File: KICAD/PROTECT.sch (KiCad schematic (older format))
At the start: 0 parts

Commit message: labels dans les blocks
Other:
- note added: "Bidir"
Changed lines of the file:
@@
 $Descr A4 11693 8268
 encoding utf-8
-Sheet 1 15
+Sheet 6 15
 Title ""
 Date ""
@@
 Comment4 ""
 $EndDescr
+Text HLabel 2700 3050 0    100  BiDi ~ 0
+IN_OUT_PWR
+Text HLabel 2700 3250 0    100  BiDi ~ 0
+VProt
+Text Notes 2300 3500 0    100  ~ 0
+Bidir
+Wire Notes Line
+	2800 2950 2800 3600
+Wire Notes Line
+	2800 3600 1600 3600
+Wire Notes Line
+	1600 3600 1600 2950
+Wire Notes Line
+	1600 2950 2800 2950
 $EndSCHEMATC

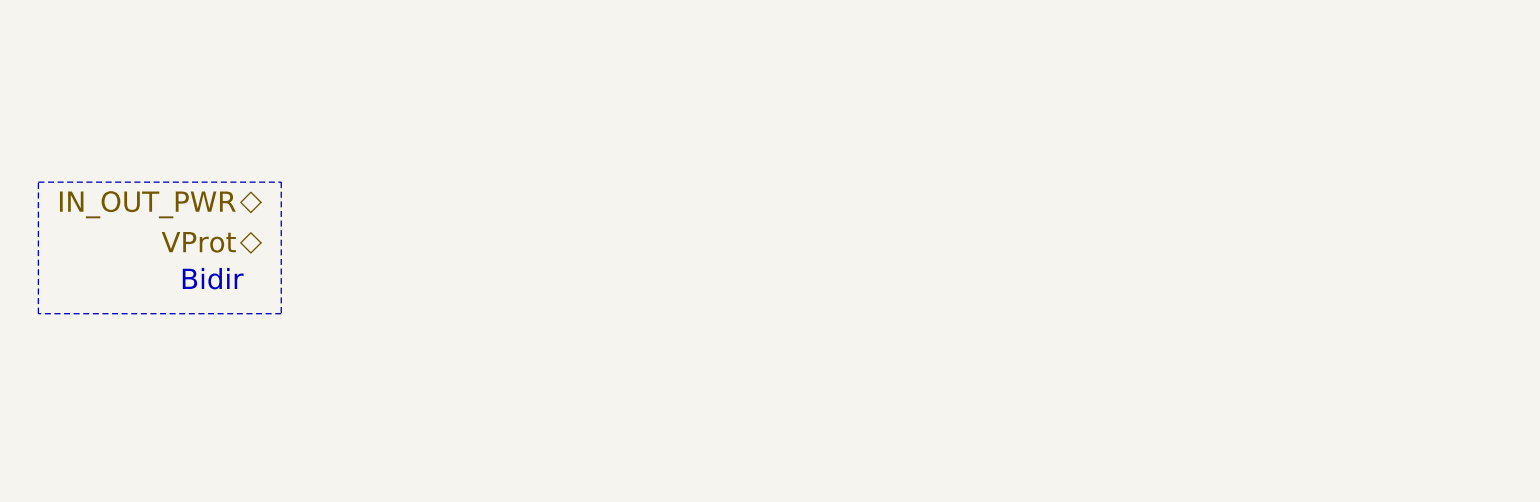
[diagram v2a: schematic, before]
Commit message: added ina240 sim + drawed protect and DC-DC chopper
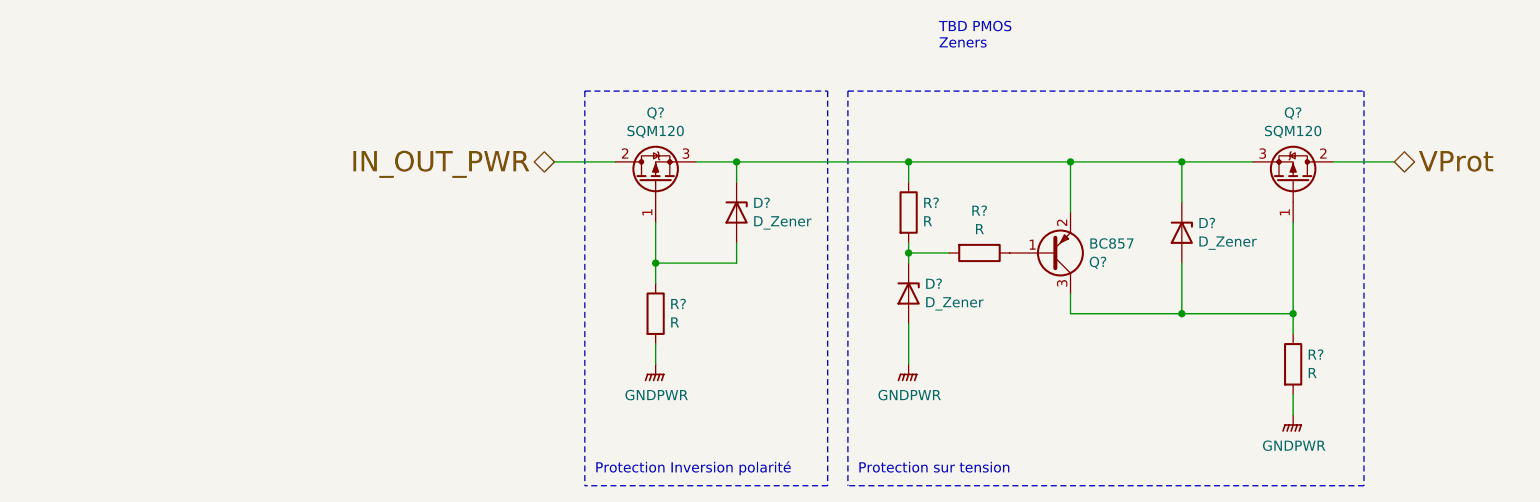
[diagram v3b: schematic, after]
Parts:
- added D? (x3): D_Zener, symbol Device:D_Zener
- added Q? (x2): SQM120, symbol Device:Q_PMOS_GDS
- added Q?: BC857, Package_TO_SOT_SMD:SOT-23, symbol Transistor_BJT:BC857
- added R? (x4): R, symbol Device:R
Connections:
- net IN_OUT_PWR: now also Q?.2 (D)
- net VProt: now also Q?.2 (D)
- new net: D?.2 (A), Q?.1 (G), R?.1
- new net: D?.1 (K), D?.1 (K), Q?.2 (E), Q?.3 (S), Q?.3 (S), R?.1
- new net: D?.2 (A), Q?.1 (G), Q?.3 (C), R?.1
- new net: Q?.1 (B), R?.1
- new net: D?.1 (K), R?.2, R?.2
- new net GNDPWR: D?.2 (A), R?.2, R?.2
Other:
- note added: "Protection Inversion polarité"
- note added: "Protection sur tension"
- note added: "TBD PMOS\nZeners\n"
- note removed: "Bidir"
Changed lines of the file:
@@
 $Descr A4 11693 8268
 encoding utf-8
-Sheet 6 15
+Sheet 5 15
 Title ""
 Date ""
 Rev ""
 Comp "ALEEA"
-Comment1 ""
+Comment1 "Dessin : Guillaume Arthaud"
 Comment2 ""
 Comment3 ""
 Comment4 ""
 $EndDescr
-Text HLabel 2700 3050 0    100  BiDi ~ 0
+Text HLabel 4150 2850 0    100  BiDi ~ 0
 IN_OUT_PWR
-Text HLabel 2700 3250 0    100  BiDi ~ 0
+Text HLabel 8300 2850 2    100  BiDi ~ 0
 VProt
-Text Notes 2300 3500 0    100  ~ 0
-Bidir
-Wire Notes Line
-	2800 2950 2800 3600
-Wire Notes Line
-	2800 3600 1600 3600
-Wire Notes Line
-	1600 3600 1600 2950
-Wire Notes Line
-	1600 2950 2800 2950
+$Comp
+L Device:Q_PMOS_GDS Q?
+U 1 1 610FCCAA
+P 4650 2950
+F 0 "Q?" V 4992 2950 50  0000 C CNN
+F 1 "SQM120" V 4901 2950 50  0000 C CNN
+F 2 "" H 4850 3050 50  0001 C CNN
+F 3 "~" H 4650 2950 50  0001 C CNN
+	1    4650 2950
+	0    -1   -1   0
+$EndComp
+$Comp
+L Device:Q_PMOS_GDS Q?
+U 1 1 610FED91
+P 7800 2950
+F 0 "Q?" V 8142 2950 50  0000 C CNN
+F 1 "SQM120" V 8051 2950 50  0000 C CNN
+F 2 "" H 8000 3050 50  0001 C CNN
+F 3 "~" H 7800 2950 50  0001 C CNN
+	1    7800 2950
+	0    1    -1   0
+$EndComp
+$Comp
+L Device:D_Zener D?
+U 1 1 61100A0F
+P 5050 3100
+F 0 "D?" V 5004 3180 50  0000 L CNN
+F 1 "D_Zener" V 5095 3180 50  0000 L CNN
+F 2 "" H 5050 3100 50  0001 C CNN
+F 3 "~" H 5050 3100 50  0001 C CNN
+	1    5050 3100
+	0    1    1    0
+$EndComp
+Wire Wire Line
+	4850 2850 5050 2850
+$Comp
+L Device:R R?
+U 1 1 61102FC8
+P 4650 3600
+F 0 "R?" H 4720 3646 50  0000 L CNN
+F 1 "R" H 4720 3555 50  0000 L CNN
+F 2 "" V 4580 3600 50  0001 C CNN
+F 3 "~" H 4650 3600 50  0001 C CNN
+	1    4650 3600
+	1    0    0    -1
+$EndComp
+Wire Wire Line
+	5050 2950 5050 2850
+Wire Wire Line
+	5050 3250 5050 3350
+Wire Wire Line
+	5050 3350 4650 3350
+Wire Wire Line
+	4650 3350 4650 3150
+Wire Wire Line
+	4650 3450 4650 3350
+Connection ~ 4650 3350
+$Comp
+L power:GNDPWR #PWR?
+U 1 1 61104B6E
+P 4650 3850
+F 0 "#PWR?" H 4650 3650 50  0001 C CNN
+F 1 "GNDPWR" H 4654 3696 50  0000 C CNN
+F 2 "" H 4650 3800 50  0001 C CNN
+F 3 "" H 4650 3800 50  0001 C CNN
+	1    4650 3850
+	1    0    0    -1
+$EndComp
+Wire Wire Line
+	4650 3850 4650 3750
+Wire Wire Line
+	4150 2850 4450 2850
+Wire Notes Line
+	4300 2500 5500 2500
+Connection ~ 5050 2850
+$Comp
+L Transistor_BJT:BC857 Q?
+U 1 1 6110710F
+P 6600 3300
+F 0 "Q?" H 6791 3346 50  0000 L CNN
+F 1 "BC857" H 6791 3255 50  0000 L CNN
+F 2 "Package_TO_SOT_SMD:SOT-23" H 6800 3225 50  0001 L CIN
+F 3 "https://www.onsemi.com/pub/Collateral/BC860-D.pdf" H 6600 3300 50  0001 L CNN
+	1    6600 3300
+	1    0    0    1
+$EndComp
+$Comp
+L Device:D_Zener D?
+U 1 1 61107C25
+P 5900 3500
+F 0 "D?" V 5854 3580 50  0000 L CNN
+F 1 "D_Zener" V 5945 3580 50  0000 L CNN
+F 2 "" H 5900 3500 50  0001 C CNN
+F 3 "~" H 5900 3500 50  0001 C CNN
+	1    5900 3500
+	0    1    1    0
+$EndComp
+$Comp
+L Device:D_Zener D?
+U 1 1 61107DEE
+P 7250 3200
+F 0 "D?" V 7204 3280 50  0000 L CNN
+F 1 "D_Zener" V 7295 3280 50  0000 L CNN
+F 2 "" H 7250 3200 50  0001 C CNN
+F 3 "~" H 7250 3200 50  0001 C CNN
+	1    7250 3200
+	0    1    1    0
+$EndComp
+$Comp
+L Device:R R?
+U 1 1 611083FB
+P 5900 3100
+F 0 "R?" H 5970 3146 50  0000 L CNN
+F 1 "R" H 5970 3055 50  0000 L CNN
+F 2 "" V 5830 3100 50  0001 C CNN
+F 3 "~" H 5900 3100 50  0001 C CNN
+	1    5900 3100
+	1    0    0    -1
+$EndComp
+Wire Wire Line
+	5900 3250 5900 3300
+Wire Wire Line
+	5900 2950 5900 2850
+Wire Wire Line
+	5050 2850 5900 2850
+$Comp
+L Device:R R?
+U 1 1 6110B925
+P 6250 3300
+F 0 "R?" V 6043 3300 50  0000 C CNN
+F 1 "R" V 6134 3300 50  0000 C CNN
+F 2 "" V 6180 3300 50  0001 C CNN
+F 3 "~" H 6250 3300 50  0001 C CNN
+	1    6250 3300
+	0    1    1    0
+$EndComp
+Wire Wire Line
+	6100 3300 5900 3300
+Connection ~ 5900 3300
+Wire Wire Line
+	5900 3300 5900 3350
+Wire Wire Line
+	5900 2850 6700 2850
+Wire Wire Line
+	6700 2850 6700 3100
+Connection ~ 5900 2850
+Wire Wire Line
+	7250 2850 6700 2850
+Connection ~ 6700 2850
+Wire Wire Line
+	6700 3600 6700 3500
+Wire Wire Line
+	7600 2850 7250 2850
+Connection ~ 7250 2850
+$Comp
+L Device:R R?
+U 1 1 61115761
+P 7800 3850
+F 0 "R?" H 7870 3896 50  0000 L CNN
+F 1 "R" H 7870 3805 50  0000 L CNN
+F 2 "" V 7730 3850 50  0001 C CNN
+F 3 "~" H 7800 3850 50  0001 C CNN
+	1    7800 3850
+	1    0    0    -1
+$EndComp
+$Comp
+L power:GNDPWR #PWR?
+U 1 1 6111576B
+P 7800 4100
+F 0 "#PWR?" H 7800 3900 50  0001 C CNN
+F 1 "GNDPWR" H 7804 3946 50  0000 C CNN
+F 2 "" H 7800 4050 50  0001 C CNN
+F 3 "" H 7800 4050 50  0001 C CNN
+	1    7800 4100
+	1    0    0    -1
+$EndComp
+Wire Wire Line
+	7800 4100 7800 4000
+$Comp
+L power:GNDPWR #PWR?
+U 1 1 611168C4
+P 5900 3850
+F 0 "#PWR?" H 5900 3650 50  0001 C CNN
+F 1 "GNDPWR" H 5904 3696 50  0000 C CNN
+F 2 "" H 5900 3800 50  0001 C CNN
+F 3 "" H 5900 3800 50  0001 C CNN
+	1    5900 3850
+	1    0    0    -1
+$EndComp
+Wire Wire Line
+	5900 3650 5900 3850
+Wire Wire Line
+	7800 3700 7800 3600
+Wire Wire Line
+	7800 3150 7800 3600
+Connection ~ 7800 3600
+Wire Wire Line
+	6700 3600 7250 3600
+Wire Wire Line
+	7250 3350 7250 3600
+Connection ~ 7250 3600
+Wire Wire Line
+	7250 3600 7800 3600
+Wire Wire Line
+	7250 2850 7250 3050
+Wire Notes Line
+	5600 2500 8150 2500
+Wire Notes Line
+	8150 4450 5600 4450
+Wire Notes Line
+	8150 2500 8150 4450
+Wire Notes Line
+	5600 2500 5600 4450
+Text Notes 5650 4400 0    50   ~ 0
+Protection sur tension
+Text Notes 4350 4400 0    50   ~ 0
+Protection Inversion polarité
+Wire Notes Line
+	5500 4450 4300 4450
+Wire Notes Line
+	5500 2500 5500 4450
+Wire Notes Line
+	4300 2500 4300 4450
+Wire Wire Line
+	8300 2850 8000 2850
+Text Notes 6050 2300 0    50   ~ 0
+TBD PMOS\nZeners\n
 $EndSCHEMATC

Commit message: a ton of new stuff. V0.8
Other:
- note added: "D2pak"
- note added: "Polarisation entre 1-5mA (15-50V)\n"
- note added: "Protection sur-tensions"
- note added: "Rapidité pas importante < 1 ms\n"
- note added: "Valeur légèrement\nsupérieure a la tension \nde coupure\nPolarisation entre 1-5 mA"
- note added: "Zeners\nThresholds faibles\n"
- note added: "chosir Res polarisation\nFaire attention puissance dissipée"
- note added: "package sod ?\nenviron 15v\n1-5mA ?"
- note removed: "Protection sur tension"
- note removed: "TBD PMOS\nZeners\n"
- moved on the sheet: D?, R?
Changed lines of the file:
@@
 $Descr A4 11693 8268
 encoding utf-8
-Sheet 6 15
+Sheet 6 16
 Title ""
 Date ""
@@
 L Device:D_Zener D?
 U 1 1 61100A0F
-P 5050 3100
+P 4950 3100
 AR Path="/614794AE/61100A0F" Ref="D?"  Part="1"
 AR Path="/61456C6A/61100A0F" Ref="D?"  Part="1"
-F 0 "D?" V 5004 3180 50  0000 L CNN
-F 1 "D_Zener" V 5095 3180 50  0000 L CNN
-F 2 "" H 5050 3100 50  0001 C CNN
-F 3 "~" H 5050 3100 50  0001 C CNN
-	1    5050 3100
-	0    1    1    0
-$EndComp
-Wire Wire Line
-	4850 2850 5050 2850
+F 0 "D?" V 4904 3180 50  0000 L CNN
+F 1 "D_Zener" V 4995 3180 50  0000 L CNN
+F 2 "" H 4950 3100 50  0001 C CNN
+F 3 "~" H 4950 3100 50  0001 C CNN
+	1    4950 3100
+	0    1    1    0
+$EndComp
 $Comp
 L Device:R R?
 U 1 1 61102FC8
-P 4650 3600
+P 4650 3700
 AR Path="/614794AE/61102FC8" Ref="R?"  Part="1"
 AR Path="/61456C6A/61102FC8" Ref="R?"  Part="1"
-F 0 "R?" H 4720 3646 50  0000 L CNN
-F 1 "R" H 4720 3555 50  0000 L CNN
-F 2 "" V 4580 3600 50  0001 C CNN
-F 3 "~" H 4650 3600 50  0001 C CNN
-	1    4650 3600
-	1    0    0    -1
-$EndComp
-Wire Wire Line
-	5050 2950 5050 2850
-Wire Wire Line
-	5050 3250 5050 3350
-Wire Wire Line
-	5050 3350 4650 3350
+F 0 "R?" H 4720 3746 50  0000 L CNN
+F 1 "R" H 4720 3655 50  0000 L CNN
+F 2 "" V 4580 3700 50  0001 C CNN
+F 3 "~" H 4650 3700 50  0001 C CNN
+	1    4650 3700
+	1    0    0    -1
+$EndComp
+Wire Wire Line
+	4950 3250 4950 3350
+Wire Wire Line
+	4950 3350 4650 3350
 Wire Wire Line
 	4650 3350 4650 3150
 Wire Wire Line
-	4650 3450 4650 3350
+	4650 3550 4650 3350
 Connection ~ 4650 3350
 $Comp
-L power:GNDPWR #PWR?
+L power:GNDPWR #PWR0121
 U 1 1 61104B6E
-P 4650 3850
-AR Path="/614794AE/61104B6E" Ref="#PWR?"  Part="1"
-AR Path="/61456C6A/61104B6E" Ref="#PWR?"  Part="1"
-F 0 "#PWR?" H 4650 3650 50  0001 C CNN
-F 1 "GNDPWR" H 4654 3696 50  0000 C CNN
-F 2 "" H 4650 3800 50  0001 C CNN
-F 3 "" H 4650 3800 50  0001 C CNN
-	1    4650 3850
-	1    0    0    -1
-$EndComp
-Wire Wire Line
-	4650 3850 4650 3750
+P 4650 4050
+AR Path="/614794AE/61104B6E" Ref="#PWR0121"  Part="1"
+AR Path="/61456C6A/61104B6E" Ref="#PWR0124"  Part="1"
+F 0 "#PWR0124" H 4650 3850 50  0001 C CNN
+F 1 "GNDPWR" H 4654 3896 50  0000 C CNN
+F 2 "" H 4650 4000 50  0001 C CNN
+F 3 "" H 4650 4000 50  0001 C CNN
+	1    4650 4050
+	1    0    0    -1
+$EndComp
+Wire Wire Line
+	4650 4050 4650 3850
 Wire Wire Line
 	4150 2850 4450 2850
 Wire Notes Line
 	4300 2500 5500 2500
-Connection ~ 5050 2850
 $Comp
 L Transistor_BJT:BC857 Q?
@@
 $Comp
 L Device:D_Zener D?
-U 1 1 61107C25
-P 5900 3500
-AR Path="/614794AE/61107C25" Ref="D?"  Part="1"
-AR Path="/61456C6A/61107C25" Ref="D?"  Part="1"
-F 0 "D?" V 5854 3580 50  0000 L CNN
-F 1 "D_Zener" V 5945 3580 50  0000 L CNN
-F 2 "" H 5900 3500 50  0001 C CNN
-F 3 "~" H 5900 3500 50  0001 C CNN
-	1    5900 3500
-	0    1    1    0
-$EndComp
-$Comp
-L Device:D_Zener D?
 U 1 1 61107DEE
 P 7250 3200
@@
 Wire Wire Line
 	5900 2950 5900 2850
-Wire Wire Line
-	5050 2850 5900 2850
 $Comp
 L Device:R R?
@@
 Wire Wire Line
 	6100 3300 5900 3300
-Connection ~ 5900 3300
-Wire Wire Line
-	5900 3300 5900 3350
 Wire Wire Line
 	5900 2850 6700 2850
@@
 $EndComp
 $Comp
-L power:GNDPWR #PWR?
+L power:GNDPWR #PWR0122
 U 1 1 6111576B
-P 7800 4100
-AR Path="/614794AE/6111576B" Ref="#PWR?"  Part="1"
-AR Path="/61456C6A/6111576B" Ref="#PWR?"  Part="1"
-F 0 "#PWR?" H 7800 3900 50  0001 C CNN
-F 1 "GNDPWR" H 7804 3946 50  0000 C CNN
-F 2 "" H 7800 4050 50  0001 C CNN
-F 3 "" H 7800 4050 50  0001 C CNN
-	1    7800 4100
-	1    0    0    -1
-$EndComp
-Wire Wire Line
-	7800 4100 7800 4000
-$Comp
-L power:GNDPWR #PWR?
-U 1 1 611168C4
-P 5900 3850
-AR Path="/614794AE/611168C4" Ref="#PWR?"  Part="1"
-AR Path="/61456C6A/611168C4" Ref="#PWR?"  Part="1"
-F 0 "#PWR?" H 5900 3650 50  0001 C CNN
-F 1 "GNDPWR" H 5904 3696 50  0000 C CNN
-F 2 "" H 5900 3800 50  0001 C CNN
-F 3 "" H 5900 3800 50  0001 C CNN
-	1    5900 3850
-	1    0    0    -1
-$EndComp
-Wire Wire Line
-	5900 3650 5900 3850
+P 7800 4050
+AR Path="/614794AE/6111576B" Ref="#PWR0122"  Part="1"
+AR Path="/61456C6A/6111576B" Ref="#PWR0125"  Part="1"
+F 0 "#PWR0125" H 7800 3850 50  0001 C CNN
+F 1 "GNDPWR" H 7804 3896 50  0000 C CNN
+F 2 "" H 7800 4000 50  0001 C CNN
+F 3 "" H 7800 4000 50  0001 C CNN
+	1    7800 4050
+	1    0    0    -1
+$EndComp
+Wire Wire Line
+	7800 4050 7800 4000
 Wire Wire Line
 	7800 3700 7800 3600
@@
 	5600 2500 5600 4450
 Text Notes 5650 4400 0    50   ~ 0
-Protection sur tension
+Protection sur-tensions
 Text Notes 4350 4400 0    50   ~ 0
 Protection Inversion polarité
@@
 Wire Wire Line
 	8300 2850 8000 2850
-Text Notes 6050 2300 0    50   ~ 0
-TBD PMOS\nZeners\n
+Text Notes 4550 2450 0    50   ~ 0
+Zeners\nThresholds faibles\n
+Text Notes 4900 2700 0    50   ~ 0
+D2pak
+Text Notes 5000 3450 0    50   ~ 0
+package sod ?\nenviron 15v\n1-5mA ?
+Text Notes 3250 3650 0    50   ~ 0
+chosir Res polarisation\nFaire attention puissance dissipée
+Wire Wire Line
+	4850 2850 4950 2850
+Wire Wire Line
+	4950 2950 4950 2850
+Connection ~ 4950 2850
+Wire Wire Line
+	4950 2850 5900 2850
+Connection ~ 5900 3300
+Wire Wire Line
+	5900 3850 5900 4050
+$Comp
+L power:GNDPWR #PWR0123
+U 1 1 611168C4
+P 5900 4050
+AR Path="/614794AE/611168C4" Ref="#PWR0123"  Part="1"
+AR Path="/61456C6A/611168C4" Ref="#PWR0126"  Part="1"
+F 0 "#PWR0126" H 5900 3850 50  0001 C CNN
+F 1 "GNDPWR" H 5904 3896 50  0000 C CNN
+F 2 "" H 5900 4000 50  0001 C CNN
+F 3 "" H 5900 4000 50  0001 C CNN
+	1    5900 4050
+	1    0    0    -1
+$EndComp
+Wire Wire Line
+	5900 3300 5900 3550
+$Comp
+L Device:D_Zener D?
+U 1 1 61107C25
+P 5900 3700
+AR Path="/614794AE/61107C25" Ref="D?"  Part="1"
+AR Path="/61456C6A/61107C25" Ref="D?"  Part="1"
+F 0 "D?" V 5854 3780 50  0000 L CNN
+F 1 "D_Zener" V 5945 3780 50  0000 L CNN
+F 2 "" H 5900 3700 50  0001 C CNN
+F 3 "~" H 5900 3700 50  0001 C CNN
+	1    5900 3700
+	0    1    1    0
+$EndComp
+Text Notes 6900 2450 0    50   ~ 0
+Rapidité pas importante < 1 ms\n
+Text Notes 6200 2800 0    50   ~ 0
+Polarisation entre 1-5mA (15-50V)\n
+Text Notes 6000 4100 0    50   ~ 0
+Valeur légèrement\nsupérieure a la tension \nde coupure\nPolarisation entre 1-5 mA
 $EndSCHEMATC

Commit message: merge nicolas & stef
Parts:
- D? (x2): value D_Zener -> MMSZ5245; footprint (none) -> Diode_SMD:D_SOD-123
- D?: value D_Zener -> MMSZ5262; footprint (none) -> Diode_SMD:D_SOD-123
- Q? (x2): footprint (none) -> Package_TO_SOT_SMD:TO-263-2
- R?: value R -> 330k; footprint (none) -> Resistor_SMD:R_0805_2012Metric_Pad1.20x1.40mm_HandSolder
- R? (x2): value R -> 100k; footprint (none) -> Resistor_SMD:R_0805_2012Metric_Pad1.20x1.40mm_HandSolder
- R?: value R -> 1M; footprint (none) -> Resistor_SMD:R_0805_2012Metric_Pad1.20x1.40mm_HandSolder
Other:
- note removed: "D2pak"
- note removed: "Polarisation entre 1-5mA (15-50V)\n"
- note removed: "Rapidité pas importante < 1 ms\n"
- note removed: "Valeur légèrement\nsupérieure a la tension \nde coupure\nPolarisation entre 1-5 mA"
- note removed: "Zeners\nThresholds faibles\n"
- note removed: "chosir Res polarisation\nFaire attention puissance dissipée"
- note removed: "package sod ?\nenviron 15v\n1-5mA ?"
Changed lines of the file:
@@
 $Descr A4 11693 8268
 encoding utf-8
-Sheet 11 16
+Sheet 12 16
 Title ""
 Date ""
@@
 F 0 "Q?" V 4992 2950 50  0000 C CNN
 F 1 "SQM120" V 4901 2950 50  0000 C CNN
-F 2 "" H 4850 3050 50  0001 C CNN
-F 3 "~" H 4650 2950 50  0001 C CNN
+F 2 "Package_TO_SOT_SMD:TO-263-2" H 4850 3050 50  0001 C CNN
+F 3 "https://www.mouser.fr/datasheet/2/427/sqm120p10-10m1l-1766828.pdf" H 4650 2950 50  0001 C CNN
 	1    4650 2950
 	0    -1   -1   0
@@
 F 0 "Q?" V 8142 2950 50  0000 C CNN
 F 1 "SQM120" V 8051 2950 50  0000 C CNN
-F 2 "" H 8000 3050 50  0001 C CNN
-F 3 "~" H 7800 2950 50  0001 C CNN
+F 2 "Package_TO_SOT_SMD:TO-263-2" H 8000 3050 50  0001 C CNN
+F 3 "https://www.mouser.fr/datasheet/2/427/sqm120p10-10m1l-1766828.pdf" H 7800 2950 50  0001 C CNN
 	1    7800 2950
 	0    1    -1   0
@@
 AR Path="/61456C6A/61100A0F" Ref="D?"  Part="1"
 F 0 "D?" V 4904 3180 50  0000 L CNN
-F 1 "D_Zener" V 4995 3180 50  0000 L CNN
-F 2 "" H 4950 3100 50  0001 C CNN
-F 3 "~" H 4950 3100 50  0001 C CNN
+F 1 "MMSZ5245" V 4995 3180 50  0000 L CNN
+F 2 "Diode_SMD:D_SOD-123" H 4950 3100 50  0001 C CNN
+F 3 "https://docs.rs-online.com/0640/0900766b814f560f.pdf" H 4950 3100 50  0001 C CNN
 	1    4950 3100
 	0    1    1    0
@@
 AR Path="/61456C6A/61102FC8" Ref="R?"  Part="1"
 F 0 "R?" H 4720 3746 50  0000 L CNN
-F 1 "R" H 4720 3655 50  0000 L CNN
-F 2 "" V 4580 3700 50  0001 C CNN
+F 1 "330k" H 4720 3655 50  0000 L CNN
+F 2 "Resistor_SMD:R_0805_2012Metric_Pad1.20x1.40mm_HandSolder" V 4580 3700 50  0001 C CNN
 F 3 "~" H 4650 3700 50  0001 C CNN
 	1    4650 3700
@@
 AR Path="/614794AE/61104B6E" Ref="#PWR0121"  Part="1"
 AR Path="/61456C6A/61104B6E" Ref="#PWR0124"  Part="1"
-F 0 "#PWR0124" H 4650 3850 50  0001 C CNN
+F 0 "#PWR0121" H 4650 3850 50  0001 C CNN
 F 1 "GNDPWR" H 4654 3896 50  0000 C CNN
 F 2 "" H 4650 4000 50  0001 C CNN
@@
 AR Path="/61456C6A/61107DEE" Ref="D?"  Part="1"
 F 0 "D?" V 7204 3280 50  0000 L CNN
-F 1 "D_Zener" V 7295 3280 50  0000 L CNN
-F 2 "" H 7250 3200 50  0001 C CNN
-F 3 "~" H 7250 3200 50  0001 C CNN
+F 1 "MMSZ5245" V 7295 3280 50  0000 L CNN
+F 2 "Diode_SMD:D_SOD-123" H 7250 3200 50  0001 C CNN
+F 3 "https://docs.rs-online.com/0640/0900766b814f560f.pdf" H 7250 3200 50  0001 C CNN
 	1    7250 3200
 	0    1    1    0
@@
 AR Path="/61456C6A/611083FB" Ref="R?"  Part="1"
 F 0 "R?" H 5970 3146 50  0000 L CNN
-F 1 "R" H 5970 3055 50  0000 L CNN
-F 2 "" V 5830 3100 50  0001 C CNN
+F 1 "100k" H 5970 3055 50  0000 L CNN
+F 2 "Resistor_SMD:R_0805_2012Metric_Pad1.20x1.40mm_HandSolder" V 5830 3100 50  0001 C CNN
 F 3 "~" H 5900 3100 50  0001 C CNN
 	1    5900 3100
@@
 AR Path="/61456C6A/6110B925" Ref="R?"  Part="1"
 F 0 "R?" V 6043 3300 50  0000 C CNN
-F 1 "R" V 6134 3300 50  0000 C CNN
-F 2 "" V 6180 3300 50  0001 C CNN
+F 1 "100k" V 6134 3300 50  0000 C CNN
+F 2 "Resistor_SMD:R_0805_2012Metric_Pad1.20x1.40mm_HandSolder" V 6180 3300 50  0001 C CNN
 F 3 "~" H 6250 3300 50  0001 C CNN
 	1    6250 3300
@@
 AR Path="/61456C6A/61115761" Ref="R?"  Part="1"
 F 0 "R?" H 7870 3896 50  0000 L CNN
-F 1 "R" H 7870 3805 50  0000 L CNN
-F 2 "" V 7730 3850 50  0001 C CNN
+F 1 "1M" H 7870 3805 50  0000 L CNN
+F 2 "Resistor_SMD:R_0805_2012Metric_Pad1.20x1.40mm_HandSolder" V 7730 3850 50  0001 C CNN
 F 3 "~" H 7800 3850 50  0001 C CNN
 	1    7800 3850
@@
 AR Path="/614794AE/6111576B" Ref="#PWR0122"  Part="1"
 AR Path="/61456C6A/6111576B" Ref="#PWR0125"  Part="1"
-F 0 "#PWR0125" H 7800 3850 50  0001 C CNN
+F 0 "#PWR0122" H 7800 3850 50  0001 C CNN
 F 1 "GNDPWR" H 7804 3896 50  0000 C CNN
 F 2 "" H 7800 4000 50  0001 C CNN
@@
 Wire Wire Line
 	8300 2850 8000 2850
-Text Notes 4550 2450 0    50   ~ 0
-Zeners\nThresholds faibles\n
-Text Notes 4900 2700 0    50   ~ 0
-D2pak
-Text Notes 5000 3450 0    50   ~ 0
-package sod ?\nenviron 15v\n1-5mA ?
-Text Notes 3250 3650 0    50   ~ 0
-chosir Res polarisation\nFaire attention puissance dissipée
 Wire Wire Line
 	4850 2850 4950 2850
@@
 AR Path="/614794AE/611168C4" Ref="#PWR0123"  Part="1"
 AR Path="/61456C6A/611168C4" Ref="#PWR0126"  Part="1"
-F 0 "#PWR0126" H 5900 3850 50  0001 C CNN
+F 0 "#PWR0123" H 5900 3850 50  0001 C CNN
 F 1 "GNDPWR" H 5904 3896 50  0000 C CNN
 F 2 "" H 5900 4000 50  0001 C CNN
@@
 AR Path="/61456C6A/61107C25" Ref="D?"  Part="1"
 F 0 "D?" V 5854 3780 50  0000 L CNN
-F 1 "D_Zener" V 5945 3780 50  0000 L CNN
-F 2 "" H 5900 3700 50  0001 C CNN
-F 3 "~" H 5900 3700 50  0001 C CNN
+F 1 "MMSZ5262" V 5945 3780 50  0000 L CNN
+F 2 "Diode_SMD:D_SOD-123" H 5900 3700 50  0001 C CNN
+F 3 "https://docs.rs-online.com/0640/0900766b814f560f.pdf" H 5900 3700 50  0001 C CNN
 	1    5900 3700
 	0    1    1    0
 $EndComp
-Text Notes 6900 2450 0    50   ~ 0
-Rapidité pas importante < 1 ms\n
-Text Notes 6200 2800 0    50   ~ 0
-Polarisation entre 1-5mA (15-50V)\n
-Text Notes 6000 4100 0    50   ~ 0
-Valeur légèrement\nsupérieure a la tension \nde coupure\nPolarisation entre 1-5 mA
 $EndSCHEMATC
